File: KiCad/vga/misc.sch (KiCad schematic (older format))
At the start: 41 parts, among them U23 LM317_TO-220

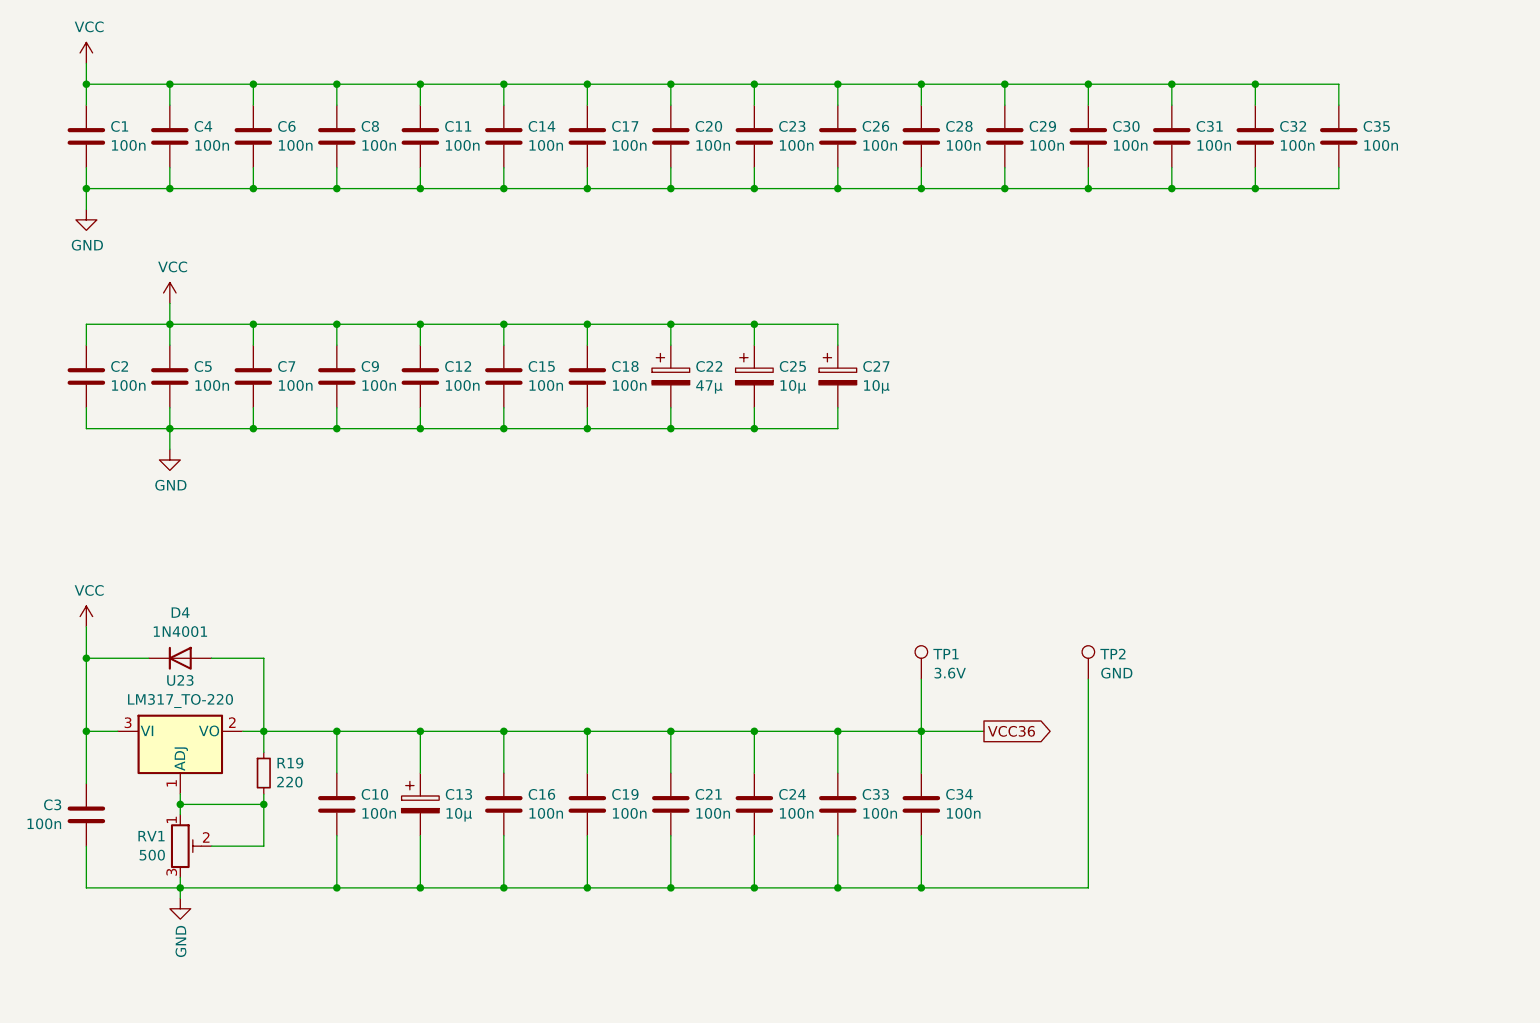
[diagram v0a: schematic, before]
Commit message: Finished VGA adapter Rev. 1.0
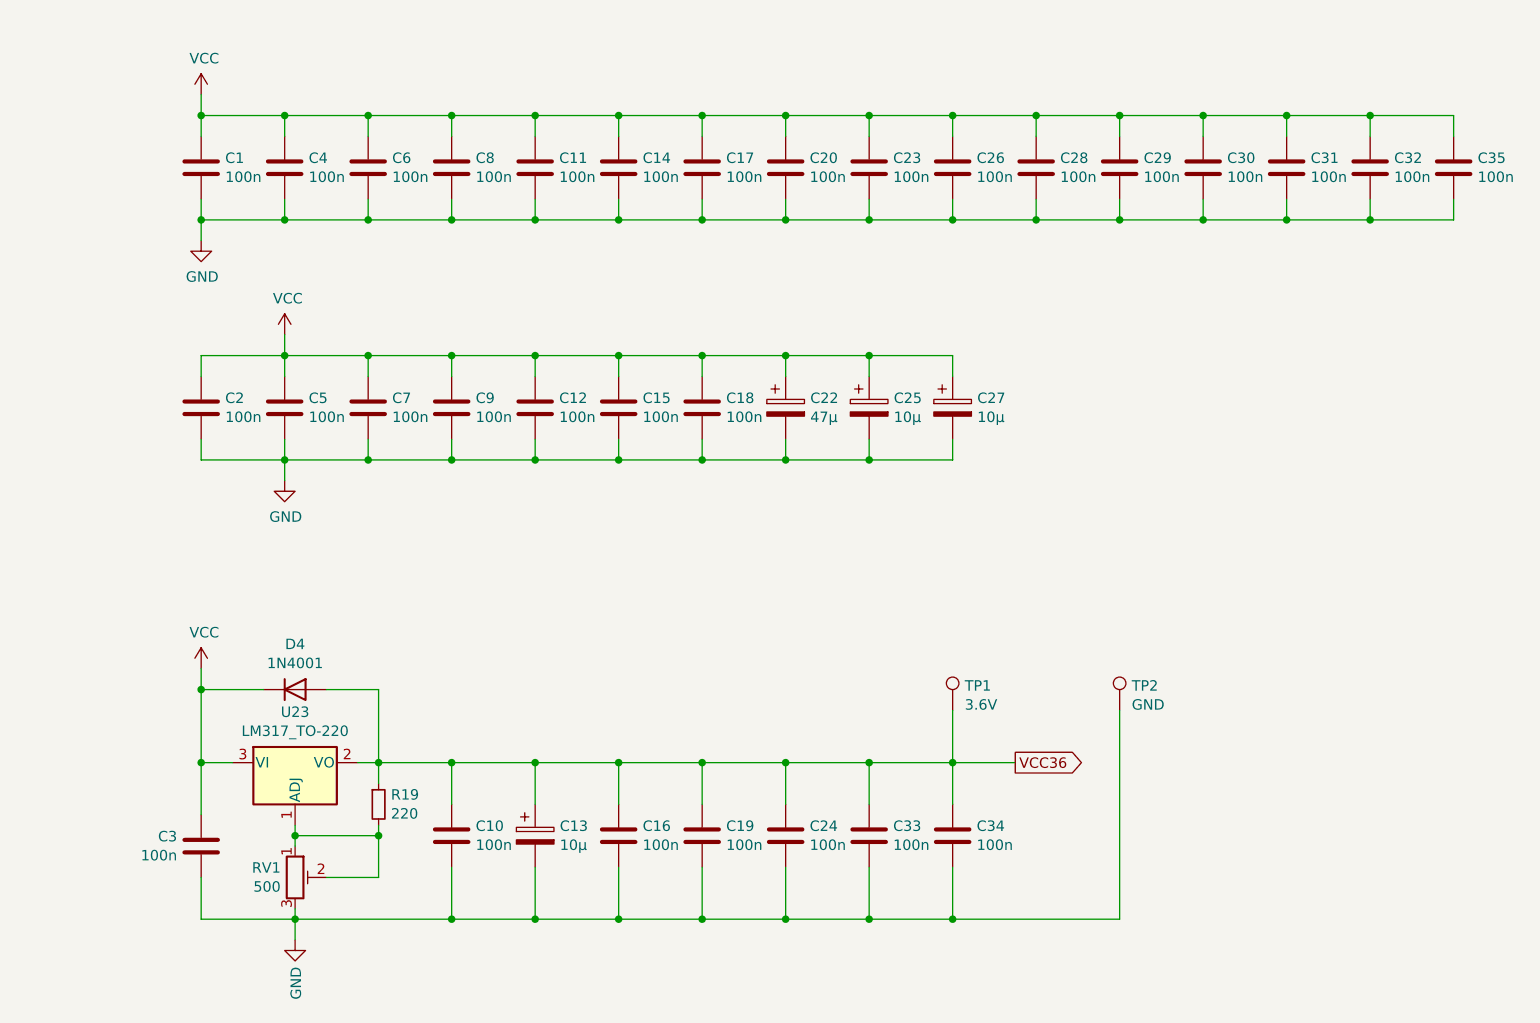
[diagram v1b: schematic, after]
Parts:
- removed C21: 100n, Capacitor_SMD:C_1206_3216Metric, symbol Device:C
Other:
- moved on the sheet: C1, C10, C11, C12, C13, C14, C15, C16, C17, C18, C19, C2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
